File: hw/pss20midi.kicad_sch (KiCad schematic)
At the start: 91 parts, among them J1 AVR-ISP, J2 Power in, J3 MIDI out, SW1 SW_Push, SW10 SW_Push, SW11 SW_Push, SW12 SW_Push, SW13 SW_Push, SW14 SW_Push, SW15 SW_Push, SW16 SW_Push, SW17 SW_Push, SW18 SW_Push, SW19 SW_Push, SW2 SW_Push, SW20 SW_Push, SW21 SW_Push, SW22 SW_Push, SW23 SW_Push, SW24 SW_Push, SW25 SW_Push, SW26 SW_Push, SW27 SW_Push, SW28 SW_Push, SW29 SW_Push, SW3 SW_Push, SW30 SW_Push, SW31 SW_Push, SW32 SW_Push, SW33 Stop, SW34 Green, SW35 Blue, SW4 SW_Push, SW5 SW_Push, SW6 SW_Push, SW7 SW_Push, SW8 SW_Push, SW9 SW_Push, U1 ATmega328PB-A, U2 74LS153, U3 74LS153, U4 74LS153, U5 74LS153, U6 MAX232, Y1 1MHz

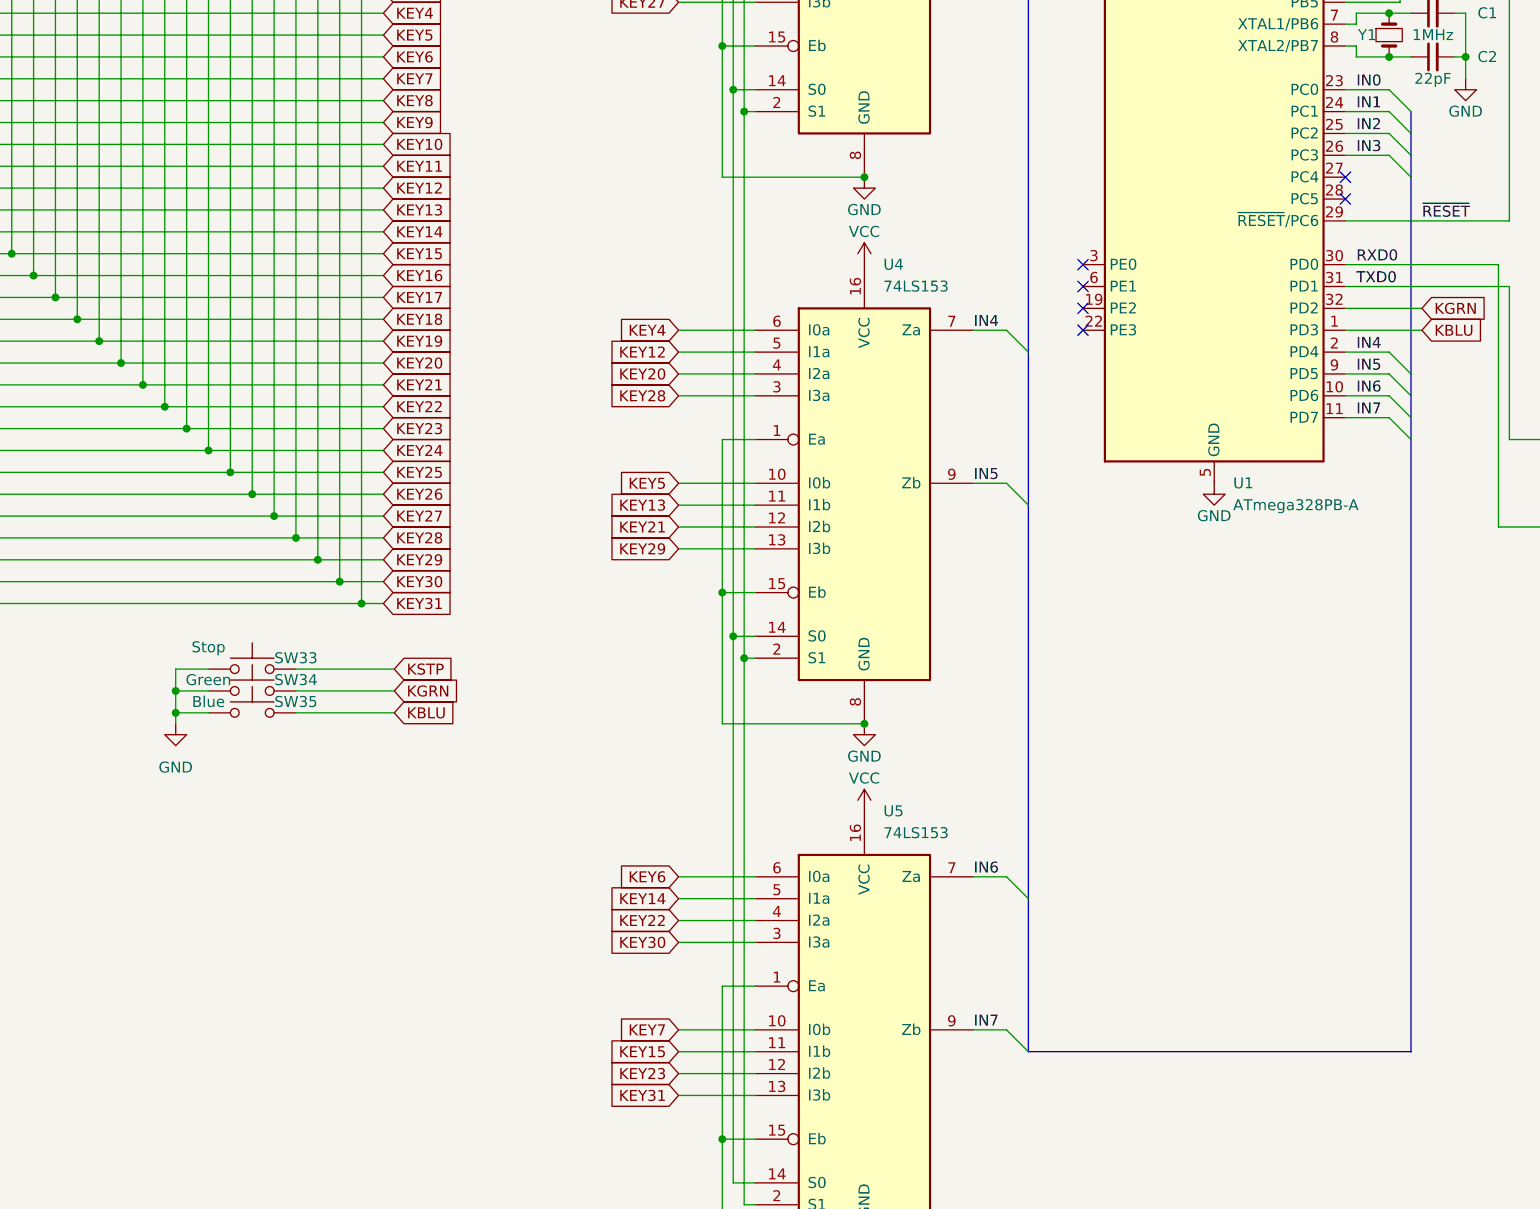
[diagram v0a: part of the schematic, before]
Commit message: completed schematic and footprint assignment
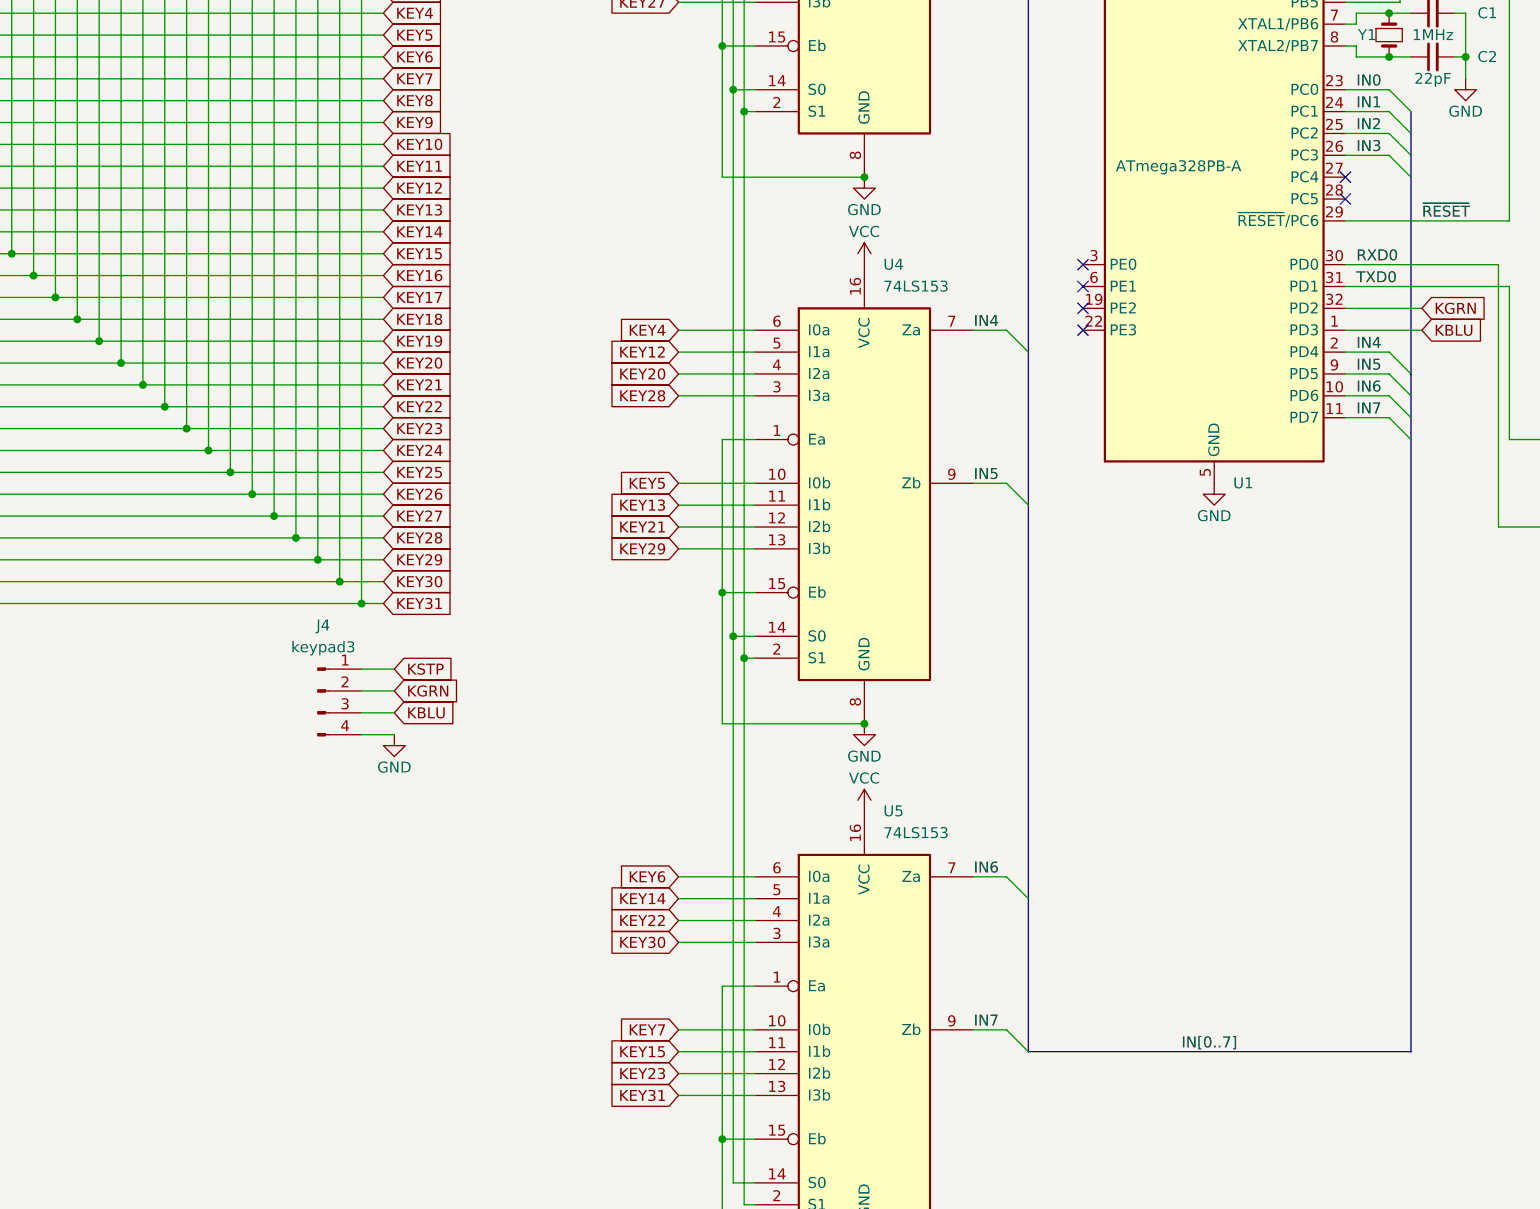
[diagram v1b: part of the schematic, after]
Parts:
- removed SW33: Stop, symbol Switch:SW_Push
- removed SW34: Green, symbol Switch:SW_Push
- removed SW35: Blue, symbol Switch:SW_Push
- added J4: keypad3, Connector_PinHeader_2.54mm:PinHeader_1x04_P2.54mm_Horizontal, symbol Connector:Conn_01x04_Pin
- C1, C10, C11, C12, C13, C2, C7, C8, C9: footprint (none) -> Capacitor_SMD:C_0805_2012Metric_Pad1.18x1.45mm_HandSolder
- C3, C4, C5, C6: footprint (none) -> Capacitor_SMD:CP_Elec_4x5.4
- J1: footprint (none) -> Connector_IDC:IDC-Header_2x03_P2.54mm_Vertical
- J2: footprint (none) -> Connector_PinHeader_2.54mm:PinHeader_1x04_P2.54mm_Horizontal
- J3: footprint (none) -> Connector_PinHeader_2.54mm:PinHeader_1x05_P2.54mm_Horizontal
- R1, R10, R11, R12, R13, R14, R15, R16, R17, R18, R19, R2, R20, R21, R22, R23, R24, R25, R26, R27, R28, R29, R3, R30, R31, R32, R33, R4, R5, R6, R7, R8, R9: footprint (none) -> Resistor_SMD:R_0805_2012Metric_Pad1.20x1.40mm_HandSolder
- SW1, SW10, SW11, SW12, SW13, SW14, SW15, SW16, SW17, SW18, SW19, SW2, SW20, SW21, SW22, SW23, SW24, SW25, SW26, SW27, SW28, SW29, SW3, SW30, SW31, SW32, SW4, SW5, SW6, SW7, SW8, SW9: footprint (none) -> pss20midi:bncontact
- U2, U3, U4, U5: footprint (none) -> Package_SO:SO-16_3.9x9.9mm_P1.27mm
- U6: footprint (none) -> Package_SO:SOIC-16_3.9x9.9mm_P1.27mm
- Y1: footprint (none) -> Crystal:Crystal_SMD_HC49-SD
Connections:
- net GND: now also J4.4 (Pin_4)
- net KBLU: now also J4.3 (Pin_3)
- net KGRN: now also J4.2 (Pin_2)
- net KSTP: now also J4.1 (Pin_1)

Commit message: PCB done
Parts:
- added C14: 1uF, Capacitor_SMD:CP_Elec_4x5.4, symbol Device:C_Polarized
- U1: value ATmega328PB-A -> ATmega328PB
- U2, U3, U4, U5: value 74LS153 -> 74HC153; footprint Package_SO:SO-16_3.9x9.9mm_P1.27mm -> Package_SO:SOIC-16_3.9x9.9mm_P1.27mm
- Y1: value 1MHz -> 4MHz
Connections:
- net GND: now also C14.2
- net KEY1: now also U2.5 (I1a); no longer U2.10 (I0b)
- net KEY10: now also U3.4 (I2a); no longer U3.5 (I1a)
- net KEY11: now also U3.3 (I3a); no longer U3.11 (I1b)
- net KEY12: now also U3.10 (I0b); no longer U4.5 (I1a)
- net KEY13: now also U3.11 (I1b); no longer U4.11 (I1b)
- net KEY14: now also U3.12 (I2b); no longer U5.5 (I1a)
- net KEY15: now also U3.13 (I3b); no longer U5.11 (I1b)
- net KEY16: now also U4.6 (I0a); no longer U2.4 (I2a)
- net KEY17: now also U4.5 (I1a); no longer U2.12 (I2b)
- net KEY18: now also U4.4 (I2a); no longer U3.4 (I2a)
- net KEY19: now also U4.3 (I3a); no longer U3.12 (I2b)
- net KEY2: now also U2.4 (I2a); no longer U3.6 (I0a)
- net KEY20: now also U4.10 (I0b); no longer U4.4 (I2a)
- net KEY21: now also U4.11 (I1b); no longer U4.12 (I2b)
- net KEY22: now also U4.12 (I2b); no longer U5.4 (I2a)
- net KEY23: now also U4.13 (I3b); no longer U5.12 (I2b)
- net KEY24: now also U5.6 (I0a); no longer U2.3 (I3a)
- net KEY25: now also U5.5 (I1a); no longer U2.13 (I3b)
- net KEY26: now also U5.4 (I2a); no longer U3.3 (I3a)
- net KEY27: now also U5.3 (I3a); no longer U3.13 (I3b)
- net KEY28: now also U5.10 (I0b); no longer U4.3 (I3a)
- net KEY29: now also U5.11 (I1b); no longer U4.13 (I3b)
- net KEY3: now also U2.3 (I3a); no longer U3.10 (I0b)
- net KEY30: now also U5.12 (I2b); no longer U5.3 (I3a)
- net KEY4: now also U2.10 (I0b); no longer U4.6 (I0a)
- net KEY5: now also U2.11 (I1b); no longer U4.10 (I0b)
- net KEY6: now also U2.12 (I2b); no longer U5.6 (I0a)
- net KEY7: now also U2.13 (I3b); no longer U5.10 (I0b)
- net KEY8: now also U3.6 (I0a); no longer U2.5 (I1a)
- net KEY9: now also U3.5 (I1a); no longer U2.11 (I1b)
- net VCC: now also C14.1
- net SEL0: now reaches U1.12 (PB0), U2.14 (S0), U3.14 (S0), U4.14 (S0), U5.14 (S0)
- net SEL1: now reaches U1.13 (PB1), U2.2 (S1), U3.2 (S1), U4.2 (S1), U5.2 (S1)
- net XTAL2: now reaches C2.1, U1.8 (XTAL2/PB7), Y1.2
- net XTAL1: now reaches C1.1, U1.7 (XTAL1/PB6), Y1.1
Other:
- moved on the sheet: C1, C2, J1, Y1

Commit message: fixed MIDI voltage and polarity mistake
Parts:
- removed C13: 0.1uF, Capacitor_SMD:C_0805_2012Metric_Pad1.18x1.45mm_HandSolder, symbol Device:C
- removed C3, C4, C5, C6: 1uF, Capacitor_SMD:CP_Elec_4x5.4, symbol Device:C_Polarized
- removed U6: MAX232, Package_SO:SOIC-16_3.9x9.9mm_P1.27mm, symbol Interface_UART:MAX232
- added J5: dbgcon, Connector_PinSocket_2.54mm:PinSocket_1x03_P2.54mm_Horizontal, symbol Connector:Conn_01x03_Socket
- added R34: 220, Resistor_SMD:R_0805_2012Metric_Pad1.20x1.40mm_HandSolder, symbol Device:R
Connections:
- net GND: now also J5.3 (Pin_3)
- net MIDI_TX: now also R34.2
- net RXD0: now also J5.1 (Pin_1)
- net TXD0: now also J5.2 (Pin_2)
- net TXD1: now also R34.1
- no-connect marks 13 -> 9
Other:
- title: (none) -> pss20midi
- moved on the sheet: J3, R33
